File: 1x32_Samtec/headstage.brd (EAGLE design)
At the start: 22.1 x 24.8 mm, 15 parts, among them U1 RHD2132_QFN

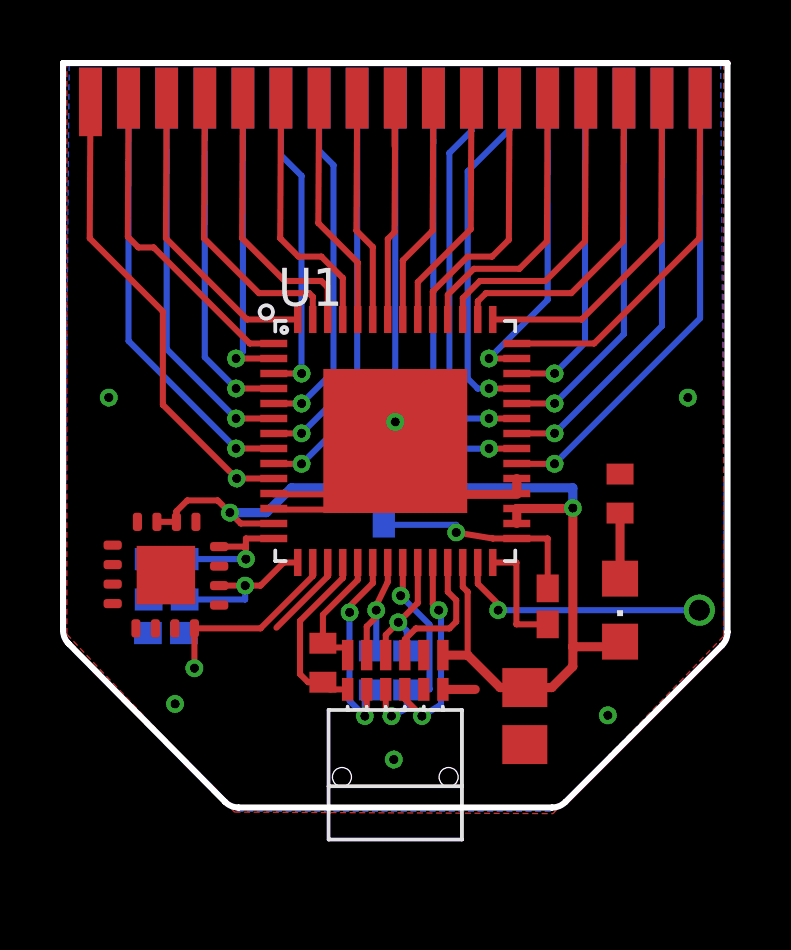
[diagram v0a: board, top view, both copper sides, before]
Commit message: Replaced samtec design with updated samtec design (2.1)
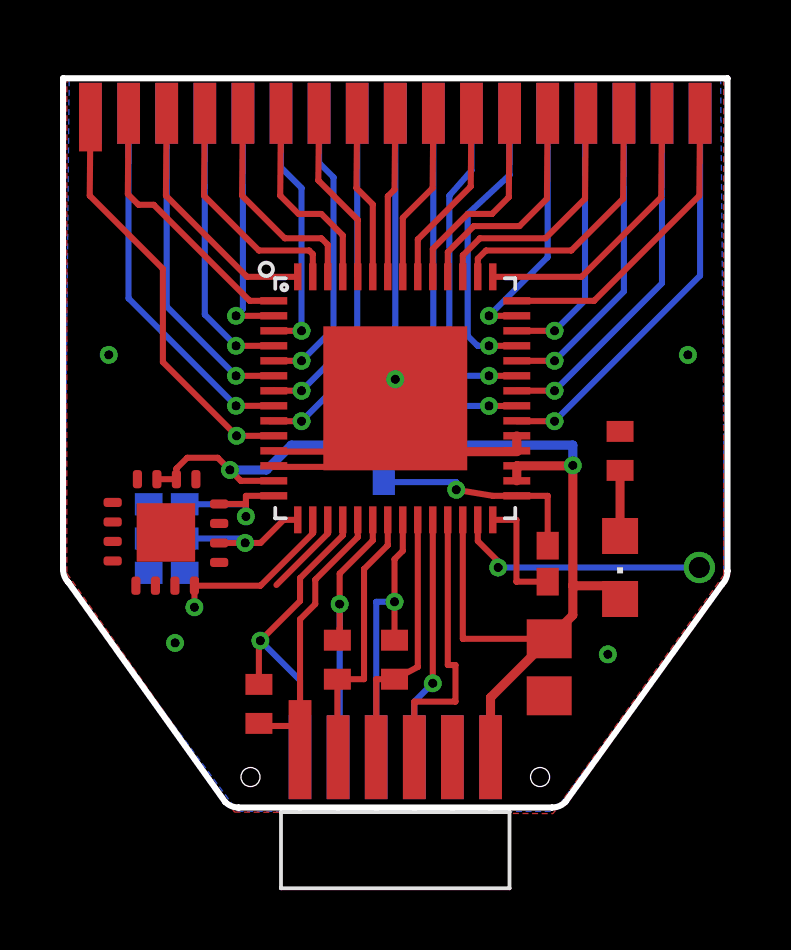
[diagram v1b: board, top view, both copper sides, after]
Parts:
- S2: value RHD2000-CABLE-AMP-SIDE -> RHD2000-CABLE-AMP-SIDEMILLMAX; device RHD2000:OMNETICS_PZN-12-AA -> RHD2000:MILLMAX-12PIN
- moved S2 4.67 mm to (11.0, -2.03)
- moved R1 2.54 mm to (6.45, 3.17), turned to 270 degrees
- moved C_Y 2.03 mm to (3.38, 8.69)
- moved C_Z 2.01 mm to (3.38, 7.54)
- moved C_X 1.83 mm to (3.38, 9.83)
- moved C_VDD 1.82 mm to (16.1, 4.39)
- moved C_REF 1.42 mm to (16.1, 7.85)
- moved U$1 1.42 mm to (3.35, 8.89)
- moved C_A 1.42 mm to (10.6, 11.2)
- moved LED1 1.42 mm to (18.5, 7.72)
- moved RLED 1.42 mm to (18.5, 11.6)
- moved U1 1.42 mm to (11.0, 13.4)
- moved R2 1.22 mm to (9.07, 4.65), flipped to the top, turned to 270 degrees
- moved R3 0.54 mm to (11.0, 4.65), flipped to the top, turned to 270 degrees
- moved U$2 0.51 mm to (11.0, 22.9)
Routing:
- net CS+: track 4.36 -> 9.86 mm
- net MISO1+: track 4.57 -> 9.54 mm
- net CS-: track 6.11 -> 11.1 mm, vias 0 -> 1
- net SCLK+: track 4.72 -> 9.16 mm, vias 1 -> 0
- net VDD: track 34.7 -> 39.1 mm
- net MOSI+: track 4.60 -> 8.99 mm, vias 1 -> 0
- net IN0: track 15.7 -> 12.8 mm
- net MOSI-: track 7.59 -> 9.92 mm, vias 2 -> 1
- net SCLK-: track 7.54 -> 9.63 mm, vias 2 -> 1
- net IN28: track 12.9 -> 11.0 mm
- net IN25: track 10.2 -> 8.32 mm
- net IN6: track 10.4 -> 8.46 mm
- net IN30: track 14.2 -> 12.3 mm
- net IN3: track 12.9 -> 11.0 mm
- net IN27: track 12.4 -> 10.5 mm
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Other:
- board size 22.1 x 24.8 mm -> 22.1 x 24.3 mm
- board text added: "Sept 2013"
- board text added: "rev 2.1 samtec"
- board text removed: "may 2013"
- board text removed: "rev 2.0 samtec"
